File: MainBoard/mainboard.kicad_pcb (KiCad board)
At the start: 2 copper layers, 32 x 40 mm, 25 parts, among them J1 Matrix_power, J2 Matrix_in, P1 USB_C_Receptacle_USB2.0_14P, Q1 AO3400A, SW1 SW_Push, U1 MCP73811T-420I-OT, U2 ESP32-C3-MINI-1, U3 LIS3DH

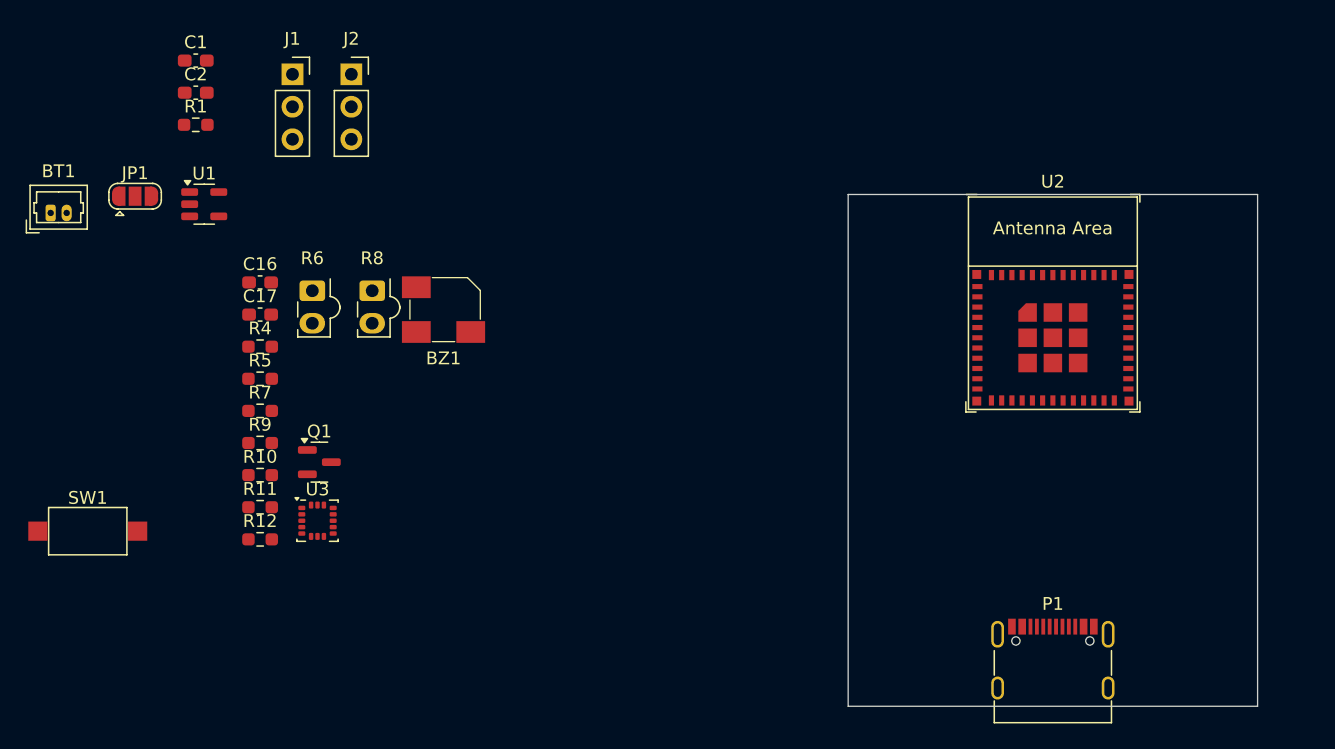
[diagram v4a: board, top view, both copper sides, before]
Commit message: Change project assumptions, create new board with esp32-c3
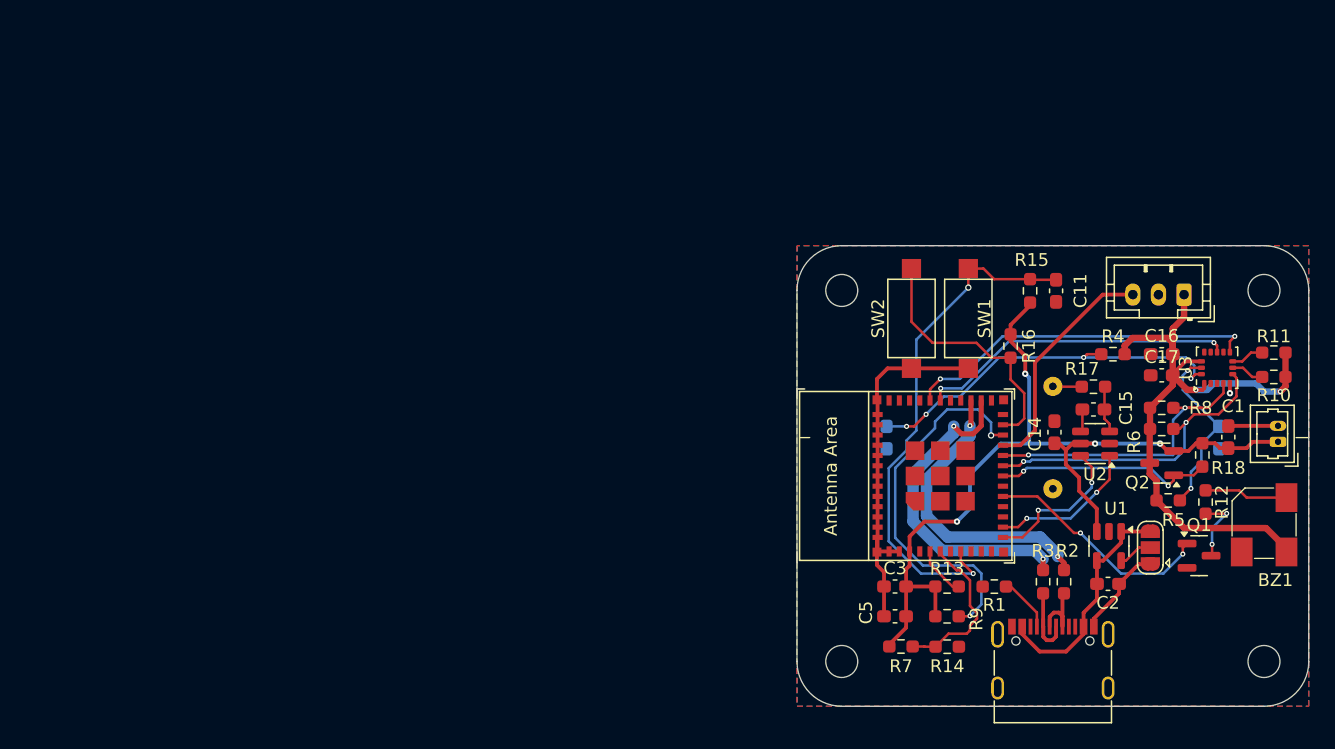
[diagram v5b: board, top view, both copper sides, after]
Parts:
- added C11: 100n, Capacitor_SMD:C_0603_1608Metric_Pad1.08x0.95mm_HandSolder, F.Cu at (230.3, 57.5)
- added C14: 100n, Capacitor_SMD:C_0603_1608Metric_Pad1.08x0.95mm_HandSolder, F.Cu at (230.1, 68.6)
- added C15: 100n, Capacitor_SMD:C_0603_1608Metric_Pad1.08x0.95mm_HandSolder, F.Cu at (233.2, 66.8)
- added C3: 100n, Capacitor_SMD:C_0603_1608Metric_Pad1.08x0.95mm_HandSolder, F.Cu at (217.7, 80.6)
- added C5: 1u, Capacitor_SMD:C_0603_1608Metric_Pad1.08x0.95mm_HandSolder, F.Cu at (217.7, 83.0)
- added H1: MountingHole_Pad, MountingHole:MountingHole_2.5mm, F.Cu at (246.5, 57.5)
- added H2: MountingHole_Pad, MountingHole:MountingHole_2.5mm, F.Cu at (213.5, 57.5)
- added H3: MountingHole_Pad, MountingHole:MountingHole_2.5mm, F.Cu at (213.5, 86.5)
- added H4: MountingHole_Pad, MountingHole:MountingHole_2.5mm, F.Cu at (246.5, 86.5)
- added Q2: AO3401A, Package_TO_SOT_SMD:SOT-23, F.Cu at (238.5, 71.0)
- added Q3: PT1921C, Diode_SMD:D_0603_1608Metric_Pad1.05x0.95mm_HandSolder, B.Cu at (243.0, 69.0)
- added Q4: PT1921C, Diode_SMD:D_0603_1608Metric_Pad1.05x0.95mm_HandSolder, B.Cu at (217.0, 69.0)
- added R13: 10k, Resistor_SMD:R_0603_1608Metric_Pad0.98x0.95mm_HandSolder, F.Cu at (221.7, 80.6)
- added R14: 10k, Resistor_SMD:R_0603_1608Metric_Pad0.98x0.95mm_HandSolder, F.Cu at (221.7, 83.0)
- added R15: 10k, Resistor_SMD:R_0603_1608Metric_Pad0.98x0.95mm_HandSolder, F.Cu at (228.2, 57.5)
- added R16: 10k, Resistor_SMD:R_0603_1608Metric_Pad0.98x0.95mm_HandSolder, F.Cu at (226.7, 61.8)
- added R17: 1k, Resistor_SMD:R_0603_1608Metric_Pad0.98x0.95mm_HandSolder, F.Cu at (233.2, 65.0)
- added R18: 47k, Resistor_SMD:R_0603_1608Metric_Pad0.98x0.95mm_HandSolder, F.Cu at (241.7, 70.4)
- added R2: 22, Resistor_SMD:R_0603_1608Metric_Pad0.98x0.95mm_HandSolder, F.Cu at (230.9, 80.3)
- added R3: 22, Resistor_SMD:R_0603_1608Metric_Pad0.98x0.95mm_HandSolder, F.Cu at (229.2, 80.3)
- added SW2: BOOT, Button_Switch_SMD:SW_SPST_CK_RS282G05A3, F.Cu at (218.9, 59.7)
- added U5: ESP32-C3-MINI-1, PCM_Espressif:ESP32-C3-MINI-1, F.Cu at (218.5, 72.0)
- J1: value Matrix_power -> touch plate; footprint Connector_PinSocket_2.54mm:PinSocket_1x03_P2.54mm_Vertical -> touch:FW-UU_05_11_28; moved to B.Cu
- J2: footprint Connector_PinSocket_2.54mm:PinSocket_1x03_P2.54mm_Vertical -> Connector_JST:JST_PH_B3B-PH-K_1x03_P2.00mm_Vertical
- R6: value PHOTO1 -> 10k; footprint OptoDevice:Osram_LPT80A -> Resistor_SMD:R_0603_1608Metric_Pad0.98x0.95mm_HandSolder
- R8: value PHOTO2 -> 10k; footprint OptoDevice:Osram_LPT80A -> Resistor_SMD:R_0603_1608Metric_Pad0.98x0.95mm_HandSolder
- SW1: value SW_Push -> ENABLE
- U2: value ESP32-C3-MINI-1 -> AT42QT1011-TSHR; footprint PCM_Espressif:ESP32-C3-MINI-1 -> Package_TO_SOT_SMD:SOT-23-6
- moved BT1 97.6 mm to (247.6, 69.3), turned to 90 degrees
- moved C1 85.9 mm to (243.7, 69.0), turned to 90 degrees
- moved JP1 84.0 mm to (237.6, 77.6), turned to 90 degrees
- moved C2 81.0 mm to (234.3, 80.4)
- moved R11 80.1 mm to (247.3, 62.4), turned to 180 degrees
- moved R10 79.6 mm to (247.3, 64.3), turned to 180 degrees
- moved U1 75.6 mm to (234.4, 77.5), turned to -90 degrees
- moved R12 74.0 mm to (241.9, 74.0), turned to -90 degrees
- moved R1 72.1 mm to (225.4, 80.6), turned to 180 degrees
- moved R5 71.6 mm to (239.0, 73.9)
- moved U3 71.3 mm to (242.8, 63.5), turned to 90 degrees
- moved SW1 70.8 mm to (223.4, 59.7), turned to 90 degrees
- moved C16 70.7 mm to (238.5, 62.5)
- moved C17 70.6 mm to (238.5, 64.1)
- moved Q1 69.1 mm to (241.4, 78.2)
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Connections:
- BZ1 pad 1: VCC -> VPP
- C16 pad 2: VCC -> VPP
- C17 pad 2: VCC -> VPP
- J1 pad 1: VCC -> Net-(J1-Pin_1)
- J2 pad 1: VCC -> VPP
- J2 pad 3: /DATA_MATRIX -> /CPU/MATRIX_DATA
- R10 pad 1: VCC -> VPP
- R11 pad 1: VCC -> VPP
- R4 pad 1: VCC -> VPP
- R5 pad 1: VCC -> VPP
- R6 pad 1: /utils/OPTO1 -> VPP
- R6 pad 2: GND -> /CPU/I2C_SDA
- R7 pad 2: /utils/BAT_LVL -> /CPU/BAT_LVL
- R8 pad 1: /utils/OPTO2 -> VPP
- R8 pad 2: GND -> /CPU/I2C_SCL
- R9 pad 1: /utils/BAT_LVL -> /CPU/BAT_LVL
- SW1 pad 2: /CPU/EN -> /CPU/BOOT_CHIP_EN
- U2 pad 1: GND -> /CPU/TOUCH
- U2 pad 3: VCC -> Net-(U2-SNSK)
- U2 pad 4: unconnected-(U2-NC-Pad4) -> Net-(U2-SNS)
- U2 pad 5: unconnected-(U2-GPIO2/ADC1_CH2-Pad5) -> VCC
- U2 pad 6: unconnected-(U2-GPIO3/ADC1_CH3-Pad6) -> /CPU/SYNC
- U3 pad 1: VCC -> VPP
- U3 pad 13: /utils/BAT_LVL -> unconnected-(U3-ADC3-Pad13)
- U3 pad 14: VCC -> VPP
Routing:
- net VCC: track 0.00 -> 71.3 mm, vias 0 -> 4
- net VPP: track 0.00 -> 51.9 mm, vias 0 -> 2
- net GND: track 0.00 -> 41.1 mm, vias 0 -> 1
- net /CPU/BOOT_CHIP_EN: track 0.00 -> 40.9 mm, vias 0 -> 2
- net /utils/OPTO1: track 0.00 -> 30.1 mm, vias 0 -> 4
- net /CPU/STRAP_GPIO8: track 0.00 -> 30.0 mm, vias 0 -> 2
- net /CPU/ACCEL_INT2: track 0.00 -> 27.8 mm, vias 0 -> 2
- net /CPU/_USB-: track 0.00 -> 25.6 mm, vias 0 -> 2
- net /CPU/I2C_SDA: track 0.00 -> 24.7 mm, vias 0 -> 2
- net /CPU/ACCEL_INT1: track 0.00 -> 24.7 mm, vias 0 -> 2
- net /CPU/I2C_SCL: track 0.00 -> 23.8 mm, vias 0 -> 2
- net /CPU/_USB+: track 0.00 -> 23.4 mm, vias 0 -> 2
- net /CPU/BOOT_GPIO9: track 0.00 -> 20.1 mm
- net +5V: track 0.00 -> 18.3 mm
- net /CPU/MATRIX_DATA: track 0.00 -> 18.2 mm
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- added copper zone on B.Cu, net GND
- added copper zone on F.Cu, net GND
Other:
- board size 32 x 40 mm -> 40 x 36 mm

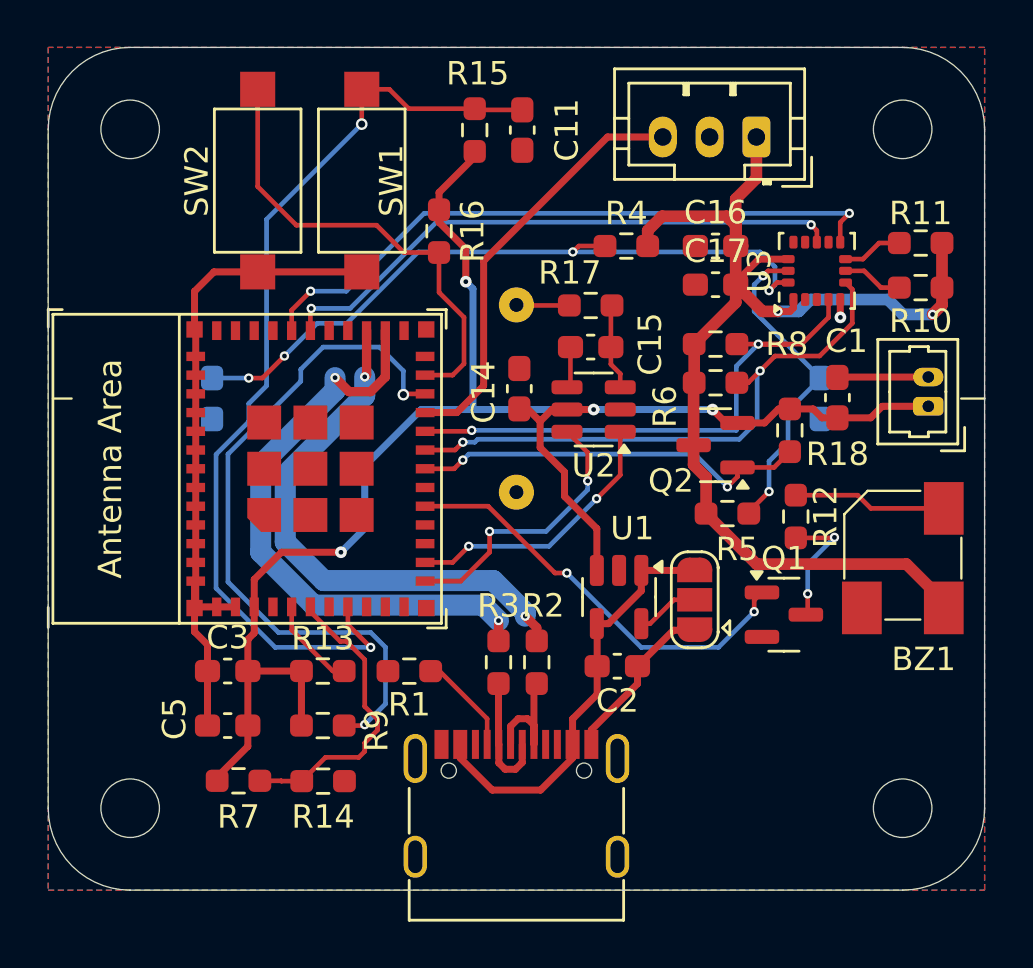
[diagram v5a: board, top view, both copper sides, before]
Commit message: Udpate project variables and add texts
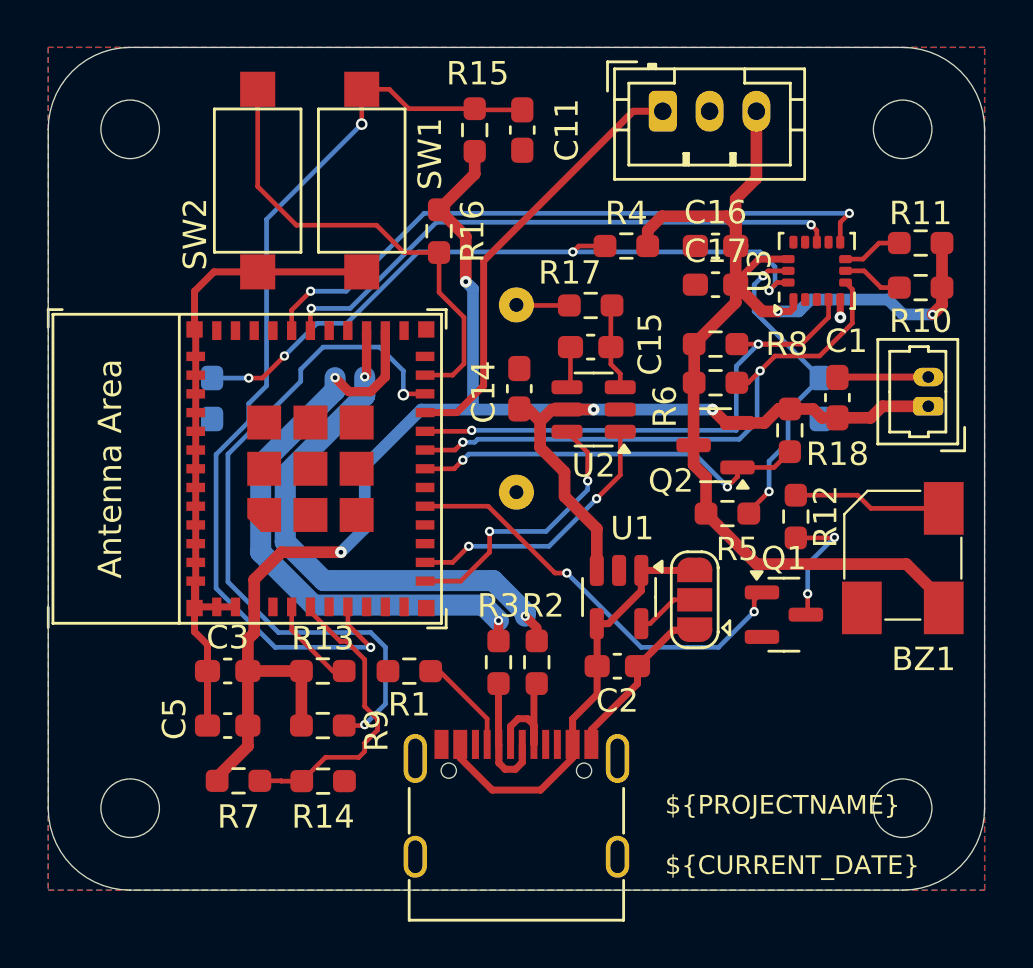
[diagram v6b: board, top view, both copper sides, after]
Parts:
- moved J2 4.15 mm to (236.3, 56.7), turned to 0 degrees
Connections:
- J2 pad 1: VPP -> /CPU/MATRIX_DATA
- J2 pad 3: /CPU/MATRIX_DATA -> VPP
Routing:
- net VPP: track 51.9 -> 53.0 mm
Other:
- board text added: "${TITLE} ${PROJECTNAME} ${REVISION} ${CURRENT_DATE}"

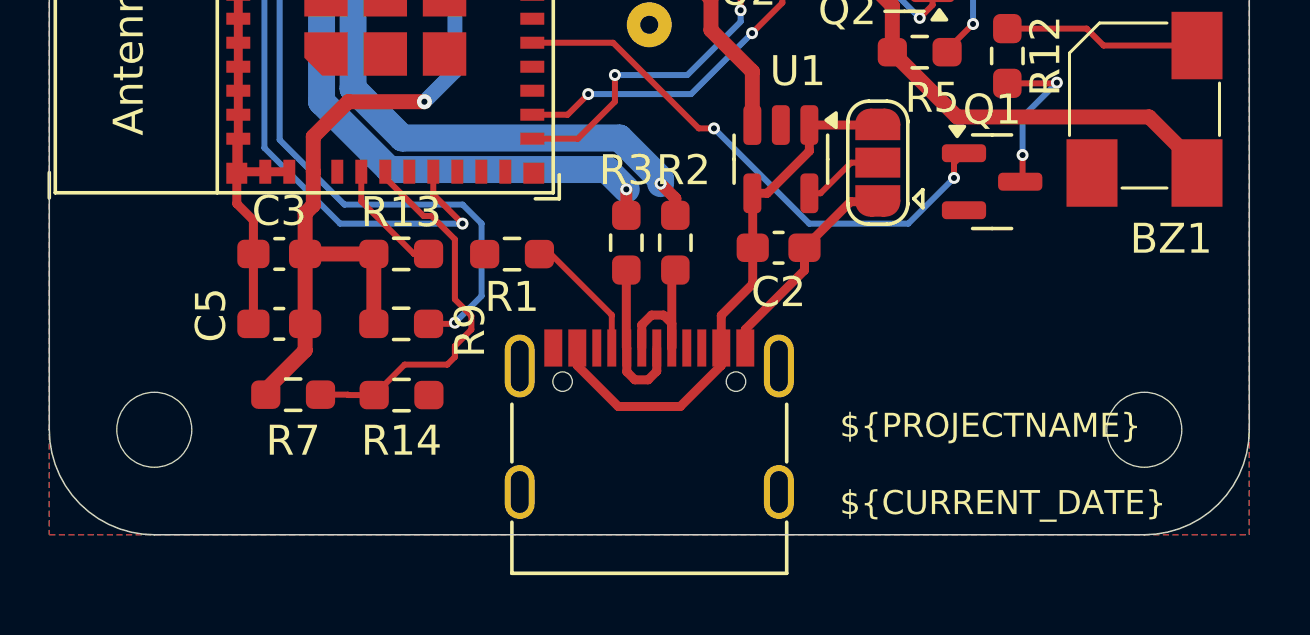
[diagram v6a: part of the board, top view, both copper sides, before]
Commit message: Change naming of project
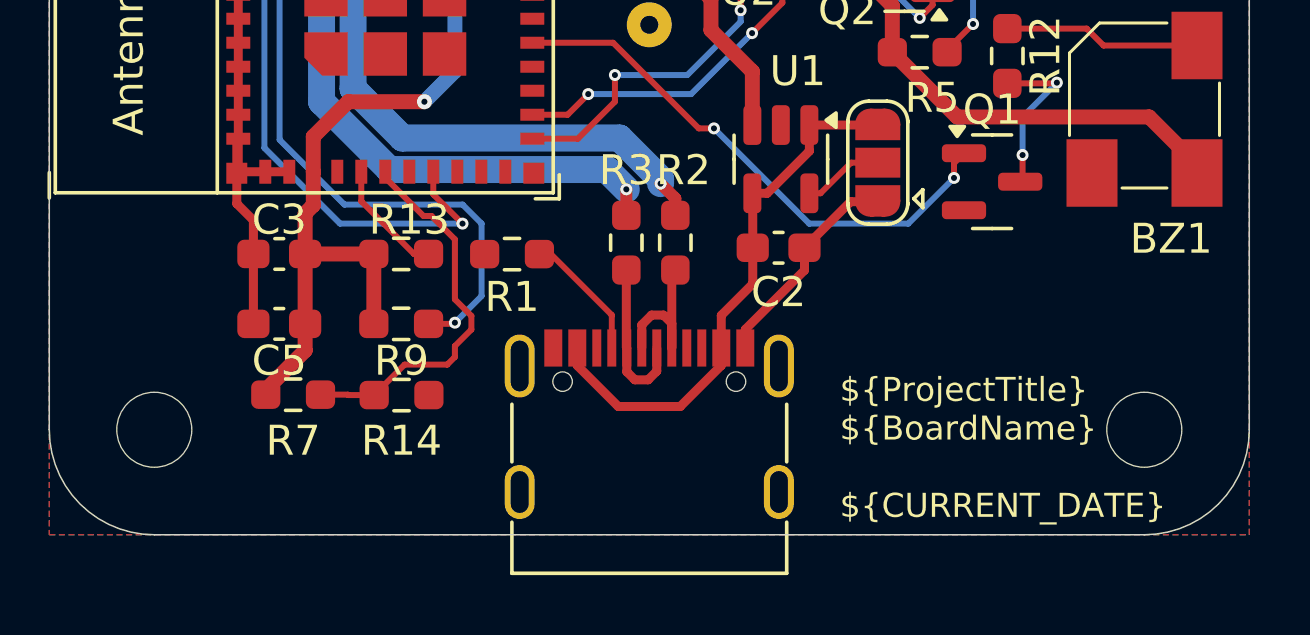
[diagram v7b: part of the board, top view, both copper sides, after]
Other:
- board text added: "${ProjectTitle} ${BoardName} ${Revision} ${CURRENT_DATE}"
- board text removed: "${TITLE} ${PROJECTNAME} ${REVISION} ${CURRENT_DATE}"
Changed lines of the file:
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@@
 		)
 	)
+	(property "BoardName" "MainBoard")
+	(property "Company" "Miłosz Derżko")
+	(property "ProjectTitle" "VirtualBlob")
+	(property "Revision" "0.4.0")
 	(net 0 "")
 	(net 1 "GND")
@@
 		(tags "resistor handsolder")
 		(property "Reference" "R13"
-			(at 0 1.39171 0)
+			(at -0.26988 1.13971 0)
 			(layer "F.SilkS")
 			(effects
@@
 		(tags "capacitor handsolder")
 		(property "Reference" "C5"
-			(at 2.27412 0.292985 90)
+			(at 0 -1.231015 0)
 			(layer "F.SilkS")
 			(effects
@@
 		(tags "capacitor handsolder")
 		(property "Reference" "C3"
-			(at 0 -1.43 0)
+			(at 0 -1.13971 0)
 			(layer "F.SilkS")
 			(effects
@@
 		(tags "resistor handsolder")
 		(property "Reference" "R9"
-			(at 2.286 -2.159 90)
+			(at 0 -1.143 180)
 			(layer "F.SilkS")
 			(effects
@@
 		(layer "Edge.Cuts")
 	)
-	(gr_text "${TITLE}\n${PROJECTNAME}\n${REVISION}\n${CURRENT_DATE}"
-		(at 236.347 89.408 0)
+	(gr_text "${ProjectTitle}\n${BoardName}\n${Revision}\n${CURRENT_DATE}"
+		(at 236.347 89.5 0)
 		(layer "F.SilkS")
 		(effects

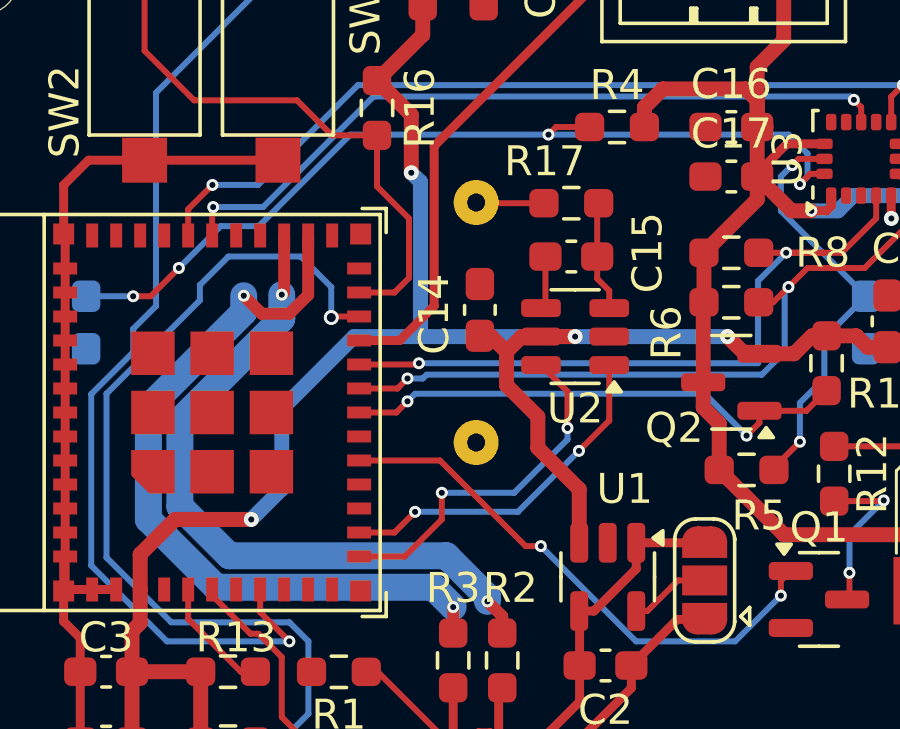
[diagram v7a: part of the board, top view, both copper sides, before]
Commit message: add new spring touch
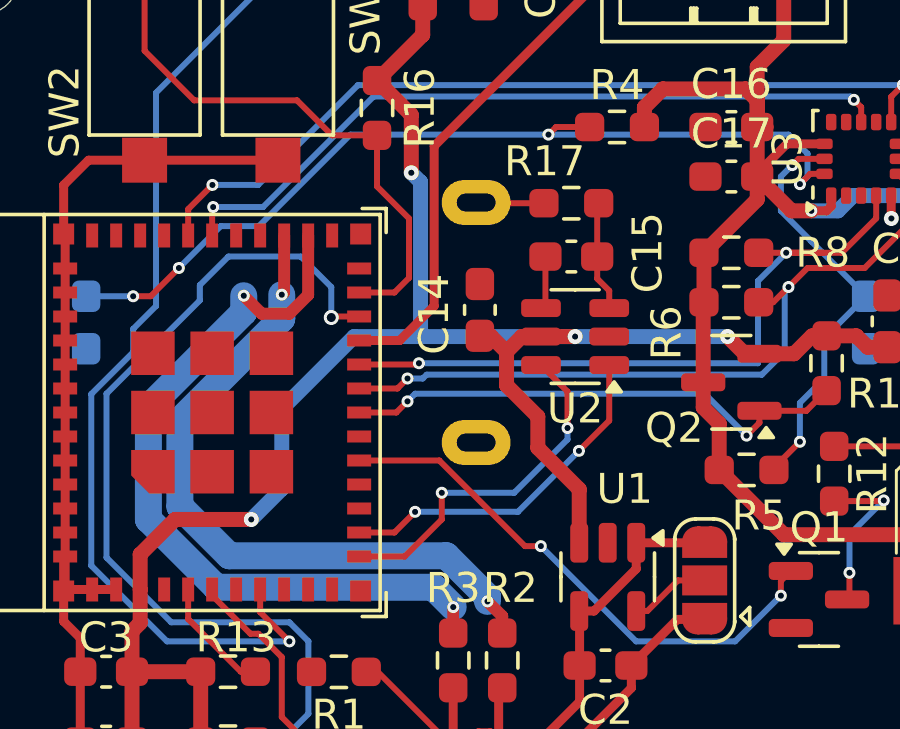
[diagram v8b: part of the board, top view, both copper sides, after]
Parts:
- removed J1: touch plate, touch:FW-UU_05_11_28
- added J3: Conn_01x02_Pin, touch:FW-UU_04_08_15, B.Cu at (230.0, 69.0)
